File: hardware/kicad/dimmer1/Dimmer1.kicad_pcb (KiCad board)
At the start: 2 copper layers, 64 x 60 mm, 30 parts, among them J100 Stapelstecker 2x20, J101 Kettenstecker, Buchse oben (S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, J102 Kettenstecker, Stift unten (S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, J103 Leistungsstecker, Buchse oben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, J104 Leistungsstecker, Stift unten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, J5 LED-Kanal 1, Q1 NCE6050KA, Q10 IRFR5305, U100 STM32C011F6P6, U101 SN74LVC1G175, U102 SN74LVC2G00DCUR, U103 SN74LVC1G08

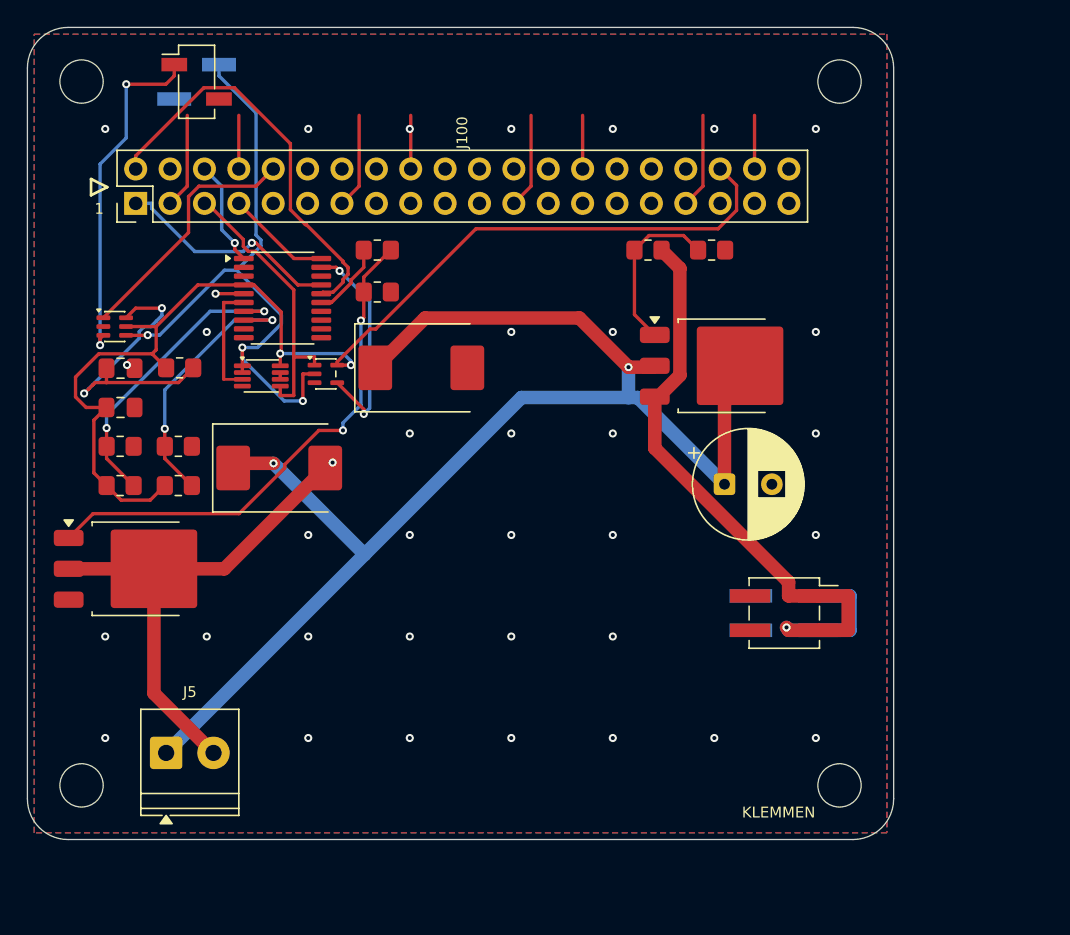
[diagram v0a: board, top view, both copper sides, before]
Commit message: Aufgabe 8b: Dimmer1 verlegt -- 0 Verletzungen, 0 offene Posten
Wurf f1_4 (vierter Wurf der dritten Serie, gebaut aus dem Stand von
e51a338). Kette wie beim Motormodul: bauen -> Vorverdrahtungs-Gate
(0 Verletzungen ohne Router) -> autoroute -> masseheiler -> DRC.

  kicad-cli pcb drc --severity-error --exit-code-violations
    Found 0 violations
    Found 0 unconnected items
  masseheiler --nur-pruefen
    alle Masseflaechen haengen zusammen, nichts zu tun
  steckerprobe spec_dimmer1
    alle elf Zeilen gruen, "Stecker sitzen auf der Vertragslage."
  pcb_checks
    Vias: 78, alle beidseitig angebunden
    ANTENNE_FREI (29.0..50.0 x 42.9..51.9): F.Cu kupferfrei

Der Router liess in diesem Wurf keine Verbindung offen; masseheiler
heilte drei Gussfragmente ueber einfache Vias.

Co-Authored-By: Claude Fable 5 <noreply@anthropic.com>
Claude-Session: https://claude.ai/code/session_01KDus95JJwCeRuwccgBWEi5
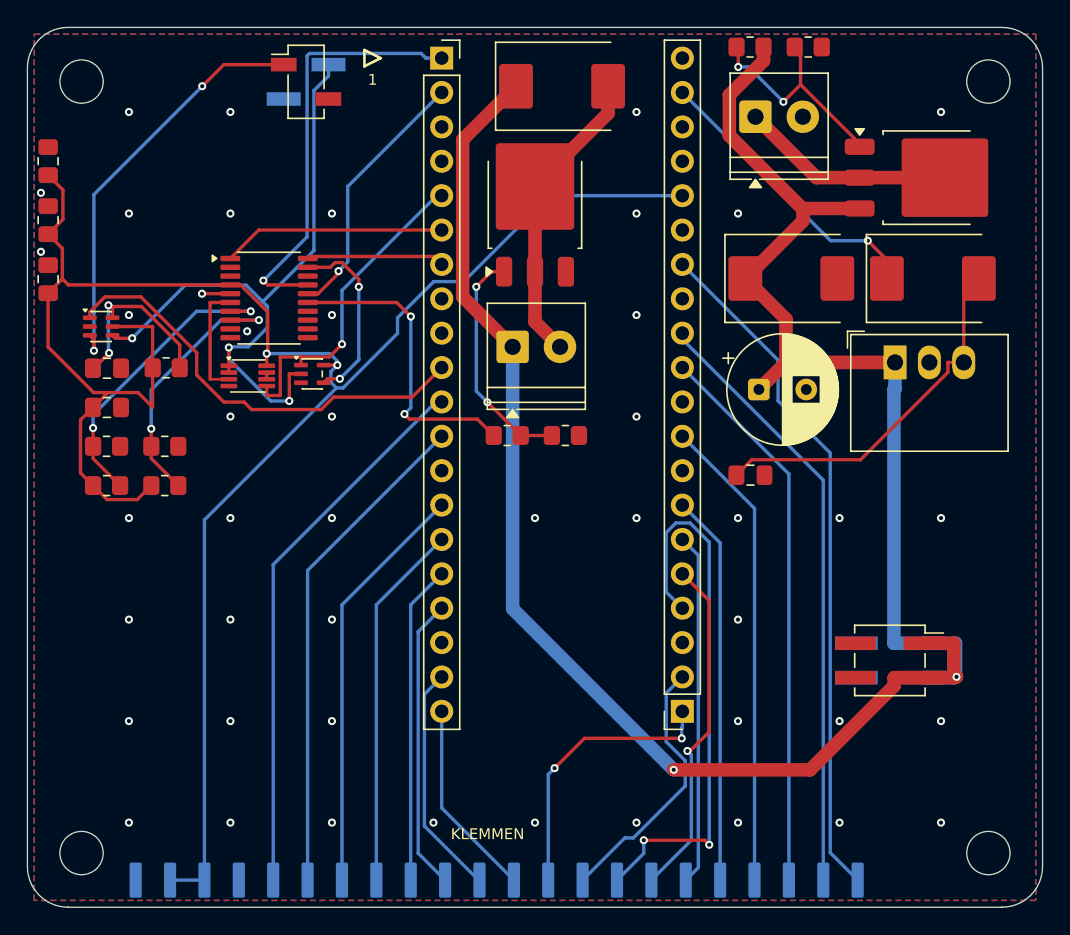
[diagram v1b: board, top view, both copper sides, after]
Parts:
- removed C12: 220u, CP_Radial_D8.0mm_P3.50mm
- removed D10: SMCJ30A, D_SMC
- removed Q10: IRFR5305, TO-252-3_TabPin2
- removed R11, R12: 10k, R_0805_2012Metric_Pad1.20x1.40mm_HandSolder
- added C102: 100n, C_0805_2012Metric_Pad1.18x1.45mm_HandSolder, F.Cu at (1.53, 9.88)
- added C103: 100n, C_0805_2012Metric_Pad1.18x1.45mm_HandSolder, F.Cu at (1.53, 14.2)
- added C104: 100n, C_0805_2012Metric_Pad1.18x1.45mm_HandSolder, F.Cu at (1.53, 18.6)
- added C90: 220u, CP_Radial_D8.0mm_P3.50mm, F.Cu at (54.0, 26.8)
- added C91: 22u, C_0805_2012Metric_Pad1.18x1.45mm_HandSolder, F.Cu at (53.4, 33.1)
- added D90: SMCJ30A, D_SMC, F.Cu at (56.4, 18.6)
- added D91: SS36C, D_SMC, F.Cu at (66.9, 18.6)
- added J105: Stapelstecker rechts, Pico-Pins 21..40 (Buchse), PinSocket_1x20_P2.54mm_Vertical, F.Cu at (48.4, 50.5)
- added J90: Versorgung Eingang, TerminalBlock_Phoenix_PT-1,5-2-3.5-H_1x02_P3.50mm_Horizontal, F.Cu at (53.8, 6.60)
- added J95: Randpads GPIO, unbestueckt (THT-Loetpad), Randpad_Reihe_1x18, B.Cu at (18.2, 63.0)
- added J96: Randpads Versorgung: 2x 3V3 + 2x GND, unbestueckt (THT-Loet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, Randpad_Reihe_1x04, B.Cu at (8.00, 63.0)
- added Q90: IRFR5305, TO-252-3_TabPin2, F.Cu at (66.5, 11.1)
- added R90: 10k, R_0805_2012Metric_Pad1.20x1.40mm_HandSolder, F.Cu at (53.4, 1.45)
- added R91: 10k, R_0805_2012Metric_Pad1.20x1.40mm_HandSolder, F.Cu at (57.7, 1.45)
- added U90: K7805-1000R3, Converter_DCDC_RECOM_R-78B-2.0_THT, F.Cu at (64.1, 24.8)
- D1: value SS36 -> SS36C
- J100: value Stapelstecker 2x20 -> Stapelstecker links, Pico-Pins 1..20 (Buchse); footprint PinHeader_2x20_P2.54mm_Vertical -> PinSocket_1x20_P2.54mm_Vertical
- Q1: value NCE6050KA -> NCE6020AK
- moved Q1 39.9 mm to (37.5, 13.0), turned to 90 degrees
- moved J5 39.4 mm to (35.9, 23.6)
- moved D1 35.1 mm to (39.5, 4.35)
- moved J100 25.0 mm to (30.6, 2.27), turned to 0 degrees
- moved RP1 17.5 mm to (39.8, 30.1)
- moved RG1 16.7 mm to (35.5, 30.1)
- moved H4 12.1 mm to (71.0, 61.0)
- moved H3 11.0 mm to (71.0, 4.00)
- moved J104 8.55 mm to (63.8, 46.8)
- moved J103 8.55 mm to (63.7, 46.8)
- moved J101 8.09 mm to (20.6, 4.02)
- moved J102 8.09 mm to (20.6, 4.02)
- moved H2 5.00 mm to (4.00, 61.0)
- moved C100 1.00 mm to (5.88, 28.1)
- moved C101 1.00 mm to (5.88, 25.2)
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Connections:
- J100 pad 11: unconnected-(J100-Pin_11-Pad11) -> /GP8
- J100 pad 12: unconnected-(J100-Pin_12-Pad12) -> /GP9
- J100 pad 14: unconnected-(J100-Pin_14-Pad14) -> /GP10
- J100 pad 15: unconnected-(J100-Pin_15-Pad15) -> /GP11
- J100 pad 16: unconnected-(J100-Pin_16-Pad16) -> /GP12
- J100 pad 17: unconnected-(J100-Pin_17-Pad17) -> /GP13
- J100 pad 19: unconnected-(J100-Pin_19-Pad19) -> /GP14
- J100 pad 20: unconnected-(J100-Pin_20-Pad20) -> /GP15
- J103 pad 1: /PWR24V -> /+24V
- J103 pad 3: /PWR24V -> /+24V
- J104 pad 1: /PWR24V -> /+24V
- J104 pad 3: /PWR24V -> /+24V
- U100 pad 10: /IN2 -> unconnected-(U100-PA3-Pad10)
- U100 pad 11: /NSLEEP -> unconnected-(U100-PA4-Pad11)
- U100 pad 12: /NFAULT -> unconnected-(U100-PA5-Pad12)
- U100 pad 13: /IPROPI -> unconnected-(U100-PA6-Pad13)
- U100 pad 9: /IN1 -> unconnected-(U100-PA2-Pad9)
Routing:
- net 3V3: track 88.1 -> 150.2 mm
- net /+24V: track 102.6 -> 162.3 mm
- net /PWR24V: track 52.4 -> 0.00 mm, vias 1 -> 0
- net /GP28: track 0.00 -> 50.9 mm
- net /GP27: track 0.00 -> 44.7 mm
- net GND: track 46.0 -> 2.09 mm, vias 35 -> 46
- net /GP18: track 0.00 -> 41.2 mm, vias 0 -> 2
- net /GP26: track 0.00 -> 41.1 mm
- net /GP8: track 0.00 -> 40.7 mm
- net /GP9: track 0.00 -> 36.9 mm
- net /GP22: track 0.00 -> 35.0 mm
- net /GP10: track 0.00 -> 30.8 mm
- net /GP21: track 0.00 -> 28.9 mm
- net /+5V_LOKAL: track 0.00 -> 27.3 mm
- net /GP11: track 0.00 -> 27.2 mm
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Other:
- board size 64 x 60 mm -> 75 x 65 mm
